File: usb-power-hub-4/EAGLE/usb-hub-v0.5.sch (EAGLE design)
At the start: 37 parts, among them U1 RICHTEKRT9715AGBR, U2 RICHTEKRT9715AGBR, U3 RICHTEKRT9715AGBR, U4 RICHTEKRT9715AGBR

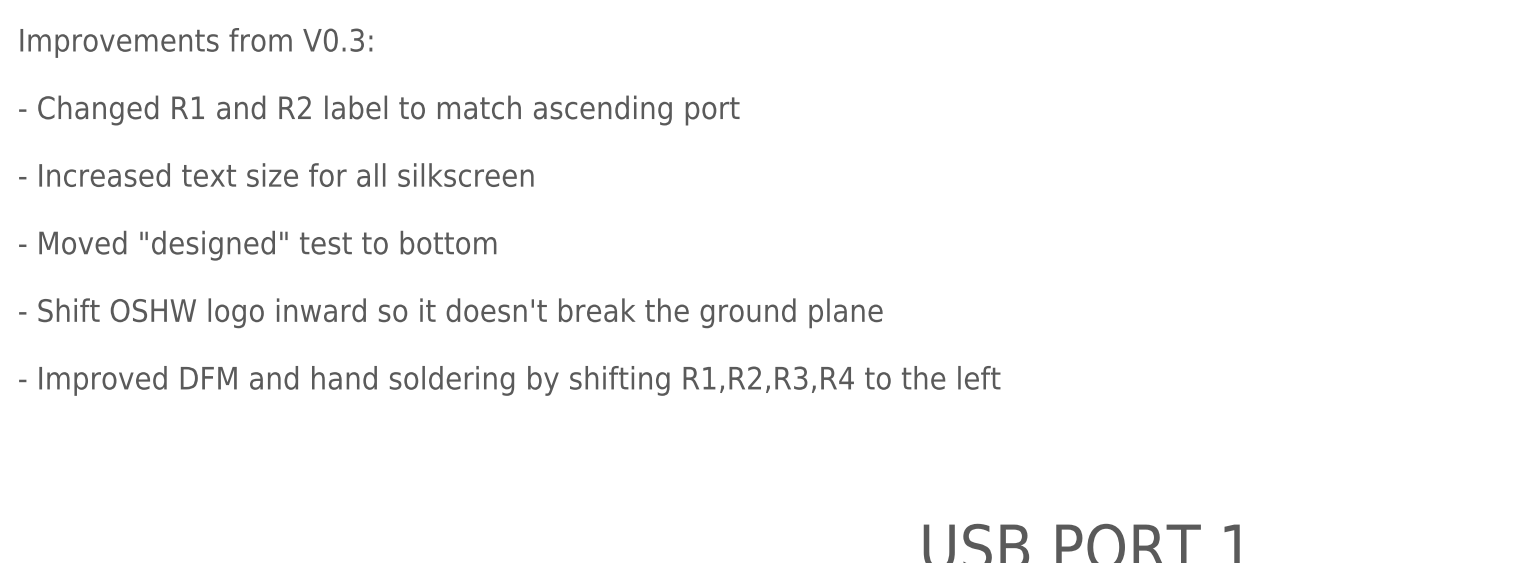
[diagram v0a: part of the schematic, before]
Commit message: V0.5 update!
Fixed an important issue of USB A through hole spacing being too
narrow.

This should be a golden version since first fabrication!
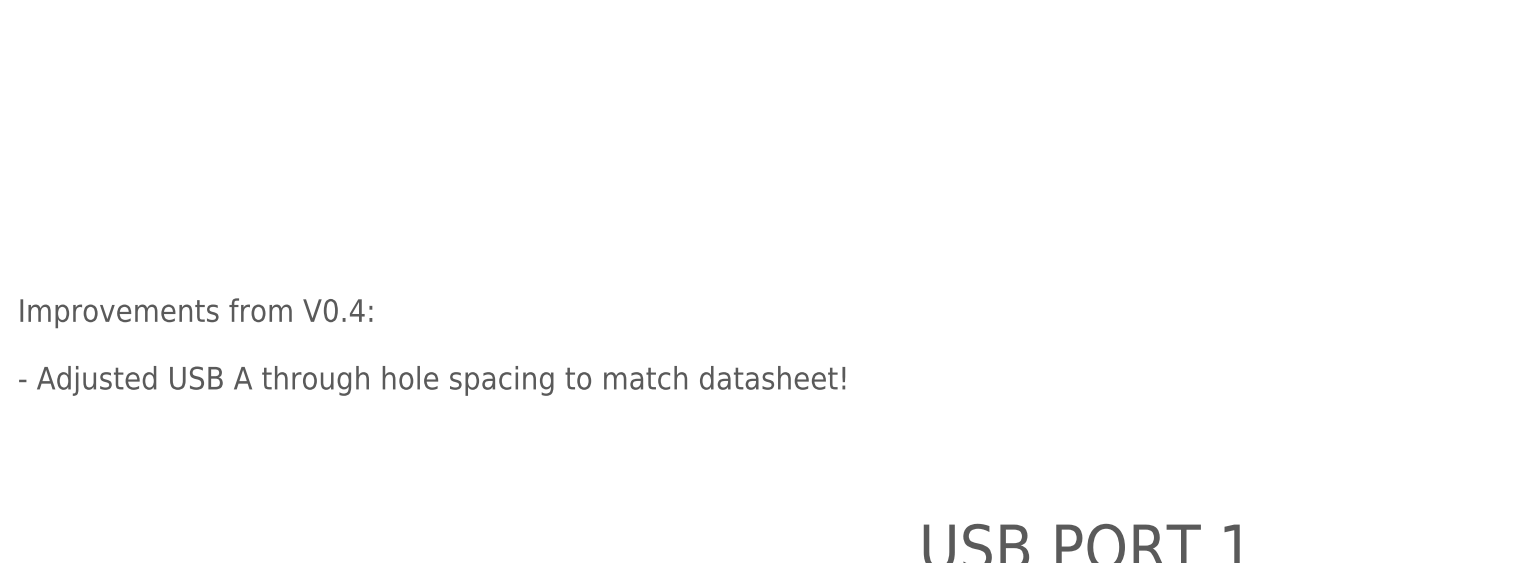
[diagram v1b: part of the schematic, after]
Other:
- note added: "Improvements from V0.4: - Adjusted USB A through hole spacing to match datasheet!"
- note removed: "Improvements from V0.3: - Changed R1 and R2 label to match ascending port - Increased text size for all silkscreen - Moved "designed" test to bottom - Shift OSHW logo inward so it doesn't break the ground plane - Improved DFM and hand soldering by shifting R1,R2,R3,R4 to the left"
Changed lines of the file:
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@@
 <attributes>
 <attribute name="CNAME" value="USB Power hub x4"/>
-<attribute name="CREVISION" value="V0.4"/>
+<attribute name="CREVISION" value="V0.5"/>
 <attribute name="DESIGNER" value="kennethlimcp"/>
 </attributes>
@@
 <wire x1="195.58" y1="30.48" x2="195.58" y2="63.5" width="0.1524" layer="97" style="shortdash"/>
 <text x="195.58" y="66.04" size="2.54" layer="97" font="vector">+5V indicator</text>
-<text x="-2.54" y="187.96" size="2.54" layer="97">Improvements from V0.3:
-- Changed R1 and R2 label to match ascending port
-- Increased text size for all silkscreen
-- Moved "designed" test to bottom
-- Shift OSHW logo inward so it doesn't break the ground plane
-- Improved DFM and hand soldering by shifting R1,R2,R3,R4 to the left </text>
+<text x="-2.54" y="187.96" size="2.54" layer="97">Improvements from V0.4:
+- Adjusted USB A through hole spacing to match datasheet!</text>
 </plain>
 <instances>
